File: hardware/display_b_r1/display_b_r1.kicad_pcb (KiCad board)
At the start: 2 copper layers, 155 x 54.5 mm, 1 part

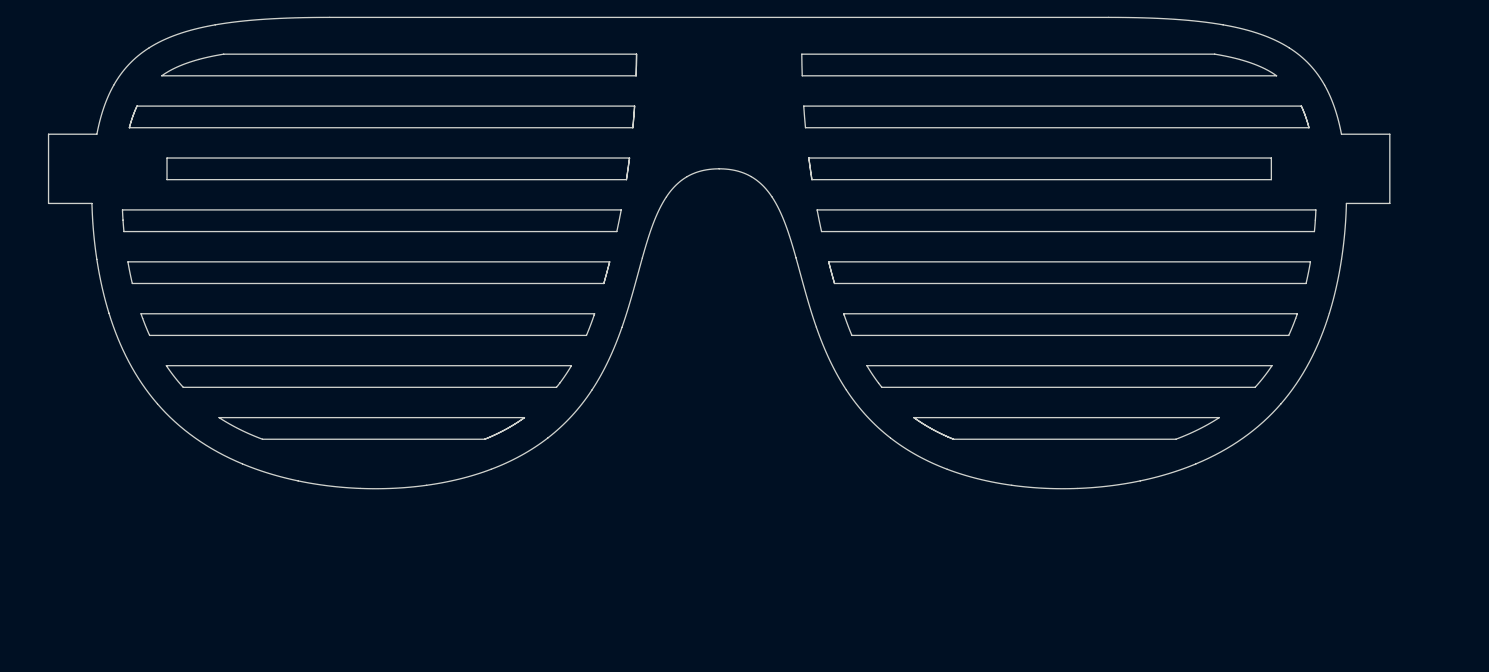
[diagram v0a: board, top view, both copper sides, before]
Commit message: Display board layout is now 95% complete, the number of caps on the board might need some further tweaking and there are also some gaps where a few more LEDs could fit. Additionally I've decided to provide the option to use the hinges as the ground connection allowing more +5V channels on the FFC connectors which should mean more current carrying capacity. The new power board schematic has had some changes, namely the vreg has changed and so have some of the passives around it, more input protect has been added, a MOV for over voltage protection and an NMOS for reverse pol. Looking at the new vreg the power dissipation before it cooks itself (~1.1W) isn't great but it's enough for about 2.5A (at around 93% eff.) for the LEDs which hasn't usually been the bottleneck (looking at you 9V batteries). This means we're expecting around 1.8A peak input current at a Vin of 7V and need to size the fuze around that as much more current and the vreg is cooked. Might look into a over voltage shutout circuit if it seems like we're blowing fuses too often.
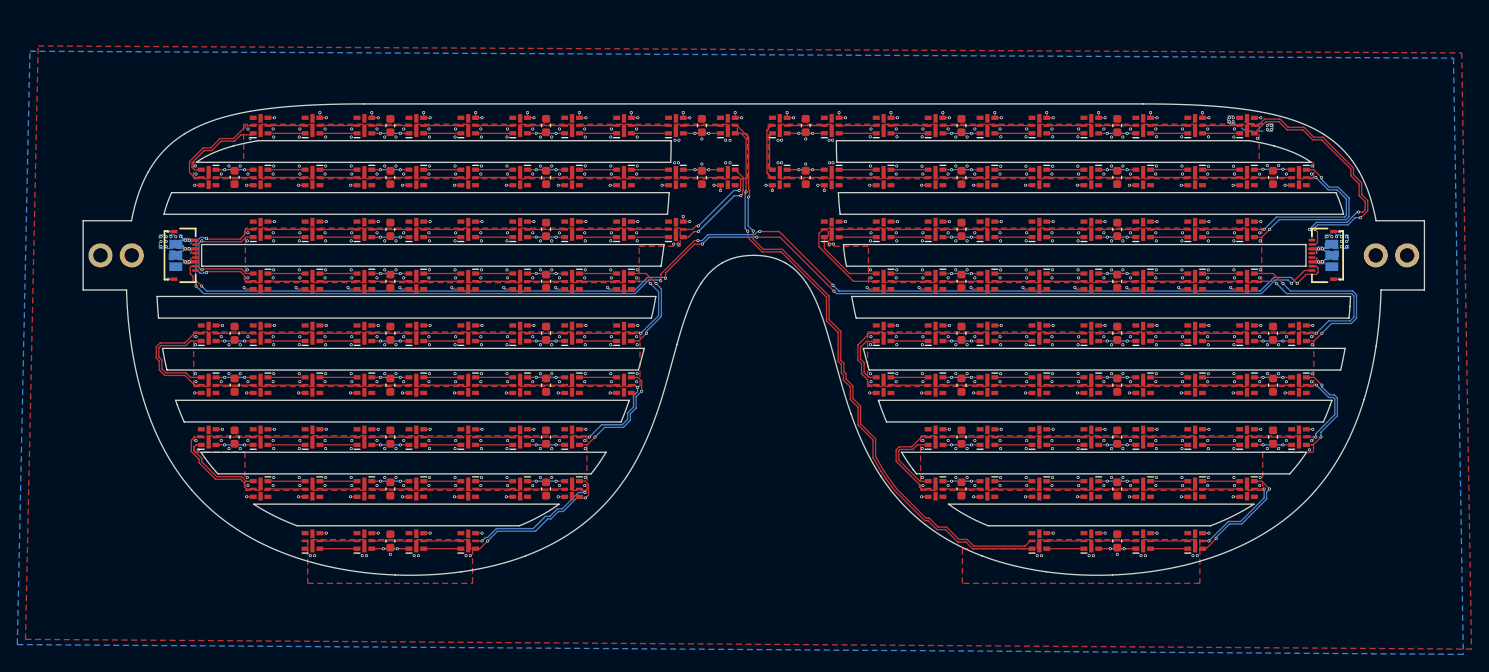
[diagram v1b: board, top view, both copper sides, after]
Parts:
- removed ?: , rave_shades:template_display_b_r1
- added C101: 22u 10V, Capacitor_SMD:C_0603_1608Metric, F.Cu at (108.0, 133.0)
- added C102: 22u 10V, Capacitor_SMD:C_0603_1608Metric, F.Cu at (192.0, 133.0)
- added C103: 22u 10V, Capacitor_SMD:C_0603_1608Metric, F.Cu at (210.0, 91.0)
- added C104: 22u 10V, Capacitor_SMD:C_0603_1608Metric, F.Cu at (108.0, 91.0)
- added C105: 22u 10V, Capacitor_SMD:C_0603_1608Metric, F.Cu at (108.0, 85.0)
- added C106: 22u 10V, Capacitor_SMD:C_0603_1608Metric, F.Cu at (108.0, 127.0)
- added C107: 22u 10V, Capacitor_SMD:C_0603_1608Metric, F.Cu at (108.0, 97.0)
- added C108: 22u 10V, Capacitor_SMD:C_0603_1608Metric, F.Cu at (108.0, 103.0)
- added C109: 22u 10V, Capacitor_SMD:C_0603_1608Metric, F.Cu at (108.0, 115.0)
- added C110: 22u 10V, Capacitor_SMD:C_0603_1608Metric, F.Cu at (192.0, 127.0)
- added C111: 22u 10V, Capacitor_SMD:C_0603_1608Metric, F.Cu at (108.0, 121.0)
- added C112: 22u 10V, Capacitor_SMD:C_0603_1608Metric, F.Cu at (192.0, 103.0)
- added C113: 22u 10V, Capacitor_SMD:C_0603_1608Metric, F.Cu at (192.0, 115.0)
- added C114: 22u 10V, Capacitor_SMD:C_0603_1608Metric, F.Cu at (108.0, 109.0)
- added C115: 22u 10V, Capacitor_SMD:C_0603_1608Metric, F.Cu at (192.0, 85.0)
- added C116: 22u 10V, Capacitor_SMD:C_0603_1608Metric, F.Cu at (192.0, 109.0)
- added C117: 22u 10V, Capacitor_SMD:C_0603_1608Metric, F.Cu at (192.0, 97.0)
- added C118: 22u 10V, Capacitor_SMD:C_0603_1608Metric, F.Cu at (192.0, 91.0)
- added C119: 22u 10V, Capacitor_SMD:C_0603_1608Metric, F.Cu at (192.0, 121.0)
- added C120: 22u 10V, Capacitor_SMD:C_0603_1608Metric, F.Cu at (174.0, 97.0)
- added C121: 22u 10V, Capacitor_SMD:C_0603_1608Metric, F.Cu at (210.0, 115.0)
- added C122: 22u 10V, Capacitor_SMD:C_0603_1608Metric, F.Cu at (174.0, 121.0)
- added C123: 22u 10V, Capacitor_SMD:C_0603_1608Metric, F.Cu at (126.0, 103.0)
- added C124: 22u 10V, Capacitor_SMD:C_0603_1608Metric, F.Cu at (126.0, 109.0)
- added C125: 22u 10V, Capacitor_SMD:C_0603_1608Metric, F.Cu at (144.0, 91.0)
- added C126: 22u 10V, Capacitor_SMD:C_0603_1608Metric, F.Cu at (90.0, 91.0)
- added C127: 22u 10V, Capacitor_SMD:C_0603_1608Metric, F.Cu at (126.0, 121.0)
- added C129: 22u 10V, Capacitor_SMD:C_0603_1608Metric, F.Cu at (90.0, 115.0)
- added C130: 22u 10V, Capacitor_SMD:C_0603_1608Metric, F.Cu at (174.0, 85.0)
- added C131: 22u 10V, Capacitor_SMD:C_0603_1608Metric, F.Cu at (174.0, 115.0)
- added C132: 22u 10V, Capacitor_SMD:C_0603_1608Metric, F.Cu at (174.0, 103.0)
- added C133: 22u 10V, Capacitor_SMD:C_0603_1608Metric, F.Cu at (126.0, 127.0)
- added C134: 22u 10V, Capacitor_SMD:C_0603_1608Metric, F.Cu at (126.0, 85.0)
- added C135: 22u 10V, Capacitor_SMD:C_0603_1608Metric, F.Cu at (156.0, 91.0)
- added C136: 22u 10V, Capacitor_SMD:C_0603_1608Metric, F.Cu at (126.0, 91.0)
- added C137: 22u 10V, Capacitor_SMD:C_0603_1608Metric, F.Cu at (156.0, 85.0)
- added C138: 22u 10V, Capacitor_SMD:C_0603_1608Metric, F.Cu at (90.0, 109.0)
- added C139: 22u 10V, Capacitor_SMD:C_0603_1608Metric, F.Cu at (174.0, 127.0)
- added C140: 22u 10V, Capacitor_SMD:C_0603_1608Metric, F.Cu at (90.0, 121.0)
- added C141: 22u 10V, Capacitor_SMD:C_0603_1608Metric, F.Cu at (210.0, 109.0)
- added C142: 22u 10V, Capacitor_SMD:C_0603_1608Metric, F.Cu at (126.0, 115.0)
- added C143: 22u 10V, Capacitor_SMD:C_0603_1608Metric, F.Cu at (174.0, 109.0)
- added C144: 22u 10V, Capacitor_SMD:C_0603_1608Metric, F.Cu at (126.0, 97.0)
- added C145: 22u 10V, Capacitor_SMD:C_0603_1608Metric, F.Cu at (210.0, 121.0)
- added C146: 22u 10V, Capacitor_SMD:C_0603_1608Metric, F.Cu at (144.0, 85.0)
- added C147: 22u 10V, Capacitor_SMD:C_0603_1608Metric, F.Cu at (174.0, 91.0)
- added D101: APA102-2020, rave_shades:LED-APA102-2020, F.Cu at (93.0, 85.0)
- added D102: APA102-2020, rave_shades:LED-APA102-2020, F.Cu at (87.0, 91.0)
- added D103: APA102-2020, rave_shades:LED-APA102-2020, F.Cu at (99.0, 97.0)
- added D104: APA102-2020, rave_shades:LED-APA102-2020, F.Cu at (93.0, 97.0)
- added D107: APA102-2020, rave_shades:LED-APA102-2020, F.Cu at (93.0, 127.0)
- added D108: APA102-2020, rave_shades:LED-APA102-2020, F.Cu at (99.0, 127.0)
- added D109: APA102-2020, rave_shades:LED-APA102-2020, F.Cu at (99.0, 85.0)
- added D110: APA102-2020, rave_shades:LED-APA102-2020, F.Cu at (93.0, 91.0)
- added D111: APA102-2020, rave_shades:LED-APA102-2020, F.Cu at (105.0, 97.0)
- added D112: APA102-2020, rave_shades:LED-APA102-2020, F.Cu at (93.0, 103.0)
- added D113: APA102-2020, rave_shades:LED-APA102-2020, F.Cu at (87.0, 109.0)
- added D114: APA102-2020, rave_shades:LED-APA102-2020, F.Cu at (87.0, 115.0)
- added D115: APA102-2020, rave_shades:LED-APA102-2020, F.Cu at (87.0, 121.0)
- added D116: APA102-2020, rave_shades:LED-APA102-2020, F.Cu at (105.0, 127.0)
- added D117: APA102-2020, rave_shades:LED-APA102-2020, F.Cu at (105.0, 85.0)
- added D118: APA102-2020, rave_shades:LED-APA102-2020, F.Cu at (99.0, 91.0)
- added D119: APA102-2020, rave_shades:LED-APA102-2020, F.Cu at (111.0, 97.0)
- added D120: APA102-2020, rave_shades:LED-APA102-2020, F.Cu at (99.0, 103.0)
- added D121: APA102-2020, rave_shades:LED-APA102-2020, F.Cu at (93.0, 109.0)
- added D122: APA102-2020, rave_shades:LED-APA102-2020, F.Cu at (93.0, 115.0)
- added D123: APA102-2020, rave_shades:LED-APA102-2020, F.Cu at (93.0, 121.0)
- added D124: APA102-2020, rave_shades:LED-APA102-2020, F.Cu at (111.0, 127.0)
- added D125: APA102-2020, rave_shades:LED-APA102-2020, F.Cu at (111.0, 85.0)
- added D126: APA102-2020, rave_shades:LED-APA102-2020, F.Cu at (105.0, 91.0)
- added D127: APA102-2020, rave_shades:LED-APA102-2020, F.Cu at (117.0, 97.0)
- added D128: APA102-2020, rave_shades:LED-APA102-2020, F.Cu at (105.0, 103.0)
- added D129: APA102-2020, rave_shades:LED-APA102-2020, F.Cu at (99.0, 109.0)
- added D130: APA102-2020, rave_shades:LED-APA102-2020, F.Cu at (99.0, 115.0)
- added D131: APA102-2020, rave_shades:LED-APA102-2020, F.Cu at (99.0, 121.0)
- added D132: APA102-2020, rave_shades:LED-APA102-2020, F.Cu at (117.0, 127.0)
- added D133: APA102-2020, rave_shades:LED-APA102-2020, F.Cu at (117.0, 85.0)
- added D134: APA102-2020, rave_shades:LED-APA102-2020, F.Cu at (111.0, 91.0)
- added D135: APA102-2020, rave_shades:LED-APA102-2020, F.Cu at (123.0, 97.0)
- added D136: APA102-2020, rave_shades:LED-APA102-2020, F.Cu at (111.0, 103.0)
- added D137: APA102-2020, rave_shades:LED-APA102-2020, F.Cu at (105.0, 109.0)
- added D138: APA102-2020, rave_shades:LED-APA102-2020, F.Cu at (105.0, 115.0)
- added D139: APA102-2020, rave_shades:LED-APA102-2020, F.Cu at (105.0, 121.0)
- added D140: APA102-2020, rave_shades:LED-APA102-2020, F.Cu at (123.0, 127.0)
- added D142: APA102-2020, rave_shades:LED-APA102-2020, F.Cu at (123.0, 85.0)
- added D143: APA102-2020, rave_shades:LED-APA102-2020, F.Cu at (117.0, 91.0)
- added D144: APA102-2020, rave_shades:LED-APA102-2020, F.Cu at (129.0, 97.0)
- added D145: APA102-2020, rave_shades:LED-APA102-2020, F.Cu at (117.0, 103.0)
- added D146: APA102-2020, rave_shades:LED-APA102-2020, F.Cu at (111.0, 109.0)
- added D147: APA102-2020, rave_shades:LED-APA102-2020, F.Cu at (111.0, 115.0)
- added D148: APA102-2020, rave_shades:LED-APA102-2020, F.Cu at (111.0, 121.0)
- added D149: APA102-2020, rave_shades:LED-APA102-2020, F.Cu at (129.0, 127.0)
- added D151: APA102-2020, rave_shades:LED-APA102-2020, F.Cu at (129.0, 85.0)
- added D152: APA102-2020, rave_shades:LED-APA102-2020, F.Cu at (123.0, 91.0)
- added D153: APA102-2020, rave_shades:LED-APA102-2020, F.Cu at (135.0, 97.0)
- added D154: APA102-2020, rave_shades:LED-APA102-2020, F.Cu at (123.0, 103.0)
- added D155: APA102-2020, rave_shades:LED-APA102-2020, F.Cu at (117.0, 109.0)
- added D156: APA102-2020, rave_shades:LED-APA102-2020, F.Cu at (117.0, 115.0)
- added D157: APA102-2020, rave_shades:LED-APA102-2020, F.Cu at (117.0, 121.0)
- added D158: APA102-2020, rave_shades:LED-APA102-2020, F.Cu at (117.0, 133.0)
- added D160: APA102-2020, rave_shades:LED-APA102-2020, F.Cu at (135.0, 85.0)
- added D161: APA102-2020, rave_shades:LED-APA102-2020, F.Cu at (129.0, 91.0)
- added D162: APA102-2020, rave_shades:LED-APA102-2020, F.Cu at (141.0, 97.0)
- added D163: APA102-2020, rave_shades:LED-APA102-2020, F.Cu at (129.0, 103.0)
- added D164: APA102-2020, rave_shades:LED-APA102-2020, F.Cu at (123.0, 109.0)
- added D165: APA102-2020, rave_shades:LED-APA102-2020, F.Cu at (123.0, 115.0)
- added D166: APA102-2020, rave_shades:LED-APA102-2020, F.Cu at (123.0, 121.0)
- added D167: APA102-2020, rave_shades:LED-APA102-2020, F.Cu at (111.0, 133.0)
- added D169: APA102-2020, rave_shades:LED-APA102-2020, F.Cu at (141.0, 85.0)
- added D170: APA102-2020, rave_shades:LED-APA102-2020, F.Cu at (135.0, 91.0)
- added D172: APA102-2020, rave_shades:LED-APA102-2020, F.Cu at (135.0, 103.0)
- added D173: APA102-2020, rave_shades:LED-APA102-2020, F.Cu at (129.0, 109.0)
- added D174: APA102-2020, rave_shades:LED-APA102-2020, F.Cu at (129.0, 115.0)
- added D175: APA102-2020, rave_shades:LED-APA102-2020, F.Cu at (129.0, 121.0)
- added D176: APA102-2020, rave_shades:LED-APA102-2020, F.Cu at (105.0, 133.0)
- added D178: APA102-2020, rave_shades:LED-APA102-2020, F.Cu at (147.0, 85.0)
- added D179: APA102-2020, rave_shades:LED-APA102-2020, F.Cu at (141.0, 91.0)
- added D180: APA102-2020, rave_shades:LED-APA102-2020, F.Cu at (147.0, 91.0)
- added D182: APA102-2020, rave_shades:LED-APA102-2020, F.Cu at (135.0, 109.0)
- added D183: APA102-2020, rave_shades:LED-APA102-2020, F.Cu at (135.0, 115.0)
- added D185: APA102-2020, rave_shades:LED-APA102-2020, F.Cu at (99.0, 133.0)
- added D187: APA102-2020, rave_shades:LED-APA102-2020, F.Cu at (153.0, 85.0)
- added D188: APA102-2020, rave_shades:LED-APA102-2020, F.Cu at (153.0, 91.0)
- added D189: APA102-2020, rave_shades:LED-APA102-2020, F.Cu at (159.0, 97.0)
- added D191: APA102-2020, rave_shades:LED-APA102-2020, F.Cu at (165.0, 109.0)
- added D192: APA102-2020, rave_shades:LED-APA102-2020, F.Cu at (165.0, 115.0)
- added D193: APA102-2020, rave_shades:LED-APA102-2020, F.Cu at (171.0, 127.0)
- added D194: APA102-2020, rave_shades:LED-APA102-2020, F.Cu at (177.0, 127.0)
- added D195: APA102-2020, rave_shades:LED-APA102-2020, F.Cu at (159.0, 85.0)
- added D196: APA102-2020, rave_shades:LED-APA102-2020, F.Cu at (159.0, 91.0)
- added D197: APA102-2020, rave_shades:LED-APA102-2020, F.Cu at (165.0, 97.0)
- added D199: APA102-2020, rave_shades:LED-APA102-2020, F.Cu at (171.0, 109.0)
- added D200: APA102-2020, rave_shades:LED-APA102-2020, F.Cu at (171.0, 115.0)
- added D202: APA102-2020, rave_shades:LED-APA102-2020, F.Cu at (183.0, 127.0)
- added D203: APA102-2020, rave_shades:LED-APA102-2020, F.Cu at (165.0, 85.0)
- added D204: APA102-2020, rave_shades:LED-APA102-2020, F.Cu at (165.0, 91.0)
- added D205: APA102-2020, rave_shades:LED-APA102-2020, F.Cu at (171.0, 97.0)
- added D206: APA102-2020, rave_shades:LED-APA102-2020, F.Cu at (165.0, 103.0)
- added D207: APA102-2020, rave_shades:LED-APA102-2020, F.Cu at (177.0, 109.0)
- added D208: APA102-2020, rave_shades:LED-APA102-2020, F.Cu at (177.0, 115.0)
- added D209: APA102-2020, rave_shades:LED-APA102-2020, F.Cu at (171.0, 121.0)
- added D210: APA102-2020, rave_shades:LED-APA102-2020, F.Cu at (189.0, 127.0)
- added D211: APA102-2020, rave_shades:LED-APA102-2020, F.Cu at (171.0, 85.0)
- added D212: APA102-2020, rave_shades:LED-APA102-2020, F.Cu at (171.0, 91.0)
- added D213: APA102-2020, rave_shades:LED-APA102-2020, F.Cu at (177.0, 97.0)
- added D214: APA102-2020, rave_shades:LED-APA102-2020, F.Cu at (171.0, 103.0)
- added D215: APA102-2020, rave_shades:LED-APA102-2020, F.Cu at (183.0, 109.0)
- added D216: APA102-2020, rave_shades:LED-APA102-2020, F.Cu at (183.0, 115.0)
- added D217: APA102-2020, rave_shades:LED-APA102-2020, F.Cu at (177.0, 121.0)
- added D218: APA102-2020, rave_shades:LED-APA102-2020, F.Cu at (195.0, 127.0)
- added D219: APA102-2020, rave_shades:LED-APA102-2020, F.Cu at (177.0, 85.0)
- added D220: APA102-2020, rave_shades:LED-APA102-2020, F.Cu at (177.0, 91.0)
- added D221: APA102-2020, rave_shades:LED-APA102-2020, F.Cu at (183.0, 97.0)
- added D222: APA102-2020, rave_shades:LED-APA102-2020, F.Cu at (177.0, 103.0)
- added D223: APA102-2020, rave_shades:LED-APA102-2020, F.Cu at (189.0, 109.0)
- added D224: APA102-2020, rave_shades:LED-APA102-2020, F.Cu at (189.0, 115.0)
- added D225: APA102-2020, rave_shades:LED-APA102-2020, F.Cu at (183.0, 121.0)
- added D226: APA102-2020, rave_shades:LED-APA102-2020, F.Cu at (201.0, 127.0)
- added D228: APA102-2020, rave_shades:LED-APA102-2020, F.Cu at (183.0, 85.0)
- added D229: APA102-2020, rave_shades:LED-APA102-2020, F.Cu at (183.0, 91.0)
- added D230: APA102-2020, rave_shades:LED-APA102-2020, F.Cu at (189.0, 97.0)
- added D231: APA102-2020, rave_shades:LED-APA102-2020, F.Cu at (183.0, 103.0)
- added D232: APA102-2020, rave_shades:LED-APA102-2020, F.Cu at (195.0, 109.0)
- added D233: APA102-2020, rave_shades:LED-APA102-2020, F.Cu at (195.0, 115.0)
- added D234: APA102-2020, rave_shades:LED-APA102-2020, F.Cu at (189.0, 121.0)
- added D235: APA102-2020, rave_shades:LED-APA102-2020, F.Cu at (207.0, 127.0)
- added D237: APA102-2020, rave_shades:LED-APA102-2020, F.Cu at (189.0, 85.0)
- added D238: APA102-2020, rave_shades:LED-APA102-2020, F.Cu at (189.0, 91.0)
- added D239: APA102-2020, rave_shades:LED-APA102-2020, F.Cu at (195.0, 97.0)
- added D240: APA102-2020, rave_shades:LED-APA102-2020, F.Cu at (189.0, 103.0)
- added D241: APA102-2020, rave_shades:LED-APA102-2020, F.Cu at (201.0, 109.0)
- added D242: APA102-2020, rave_shades:LED-APA102-2020, F.Cu at (201.0, 115.0)
- added D243: APA102-2020, rave_shades:LED-APA102-2020, F.Cu at (195.0, 121.0)
- added D244: APA102-2020, rave_shades:LED-APA102-2020, F.Cu at (201.0, 133.0)
- added D246: APA102-2020, rave_shades:LED-APA102-2020, F.Cu at (195.0, 85.0)
- added D247: APA102-2020, rave_shades:LED-APA102-2020, F.Cu at (195.0, 91.0)
- added D248: APA102-2020, rave_shades:LED-APA102-2020, F.Cu at (201.0, 97.0)
- added D249: APA102-2020, rave_shades:LED-APA102-2020, F.Cu at (195.0, 103.0)
- added D250: APA102-2020, rave_shades:LED-APA102-2020, F.Cu at (207.0, 109.0)
- added D251: APA102-2020, rave_shades:LED-APA102-2020, F.Cu at (207.0, 115.0)
- added D252: APA102-2020, rave_shades:LED-APA102-2020, F.Cu at (201.0, 121.0)
- added D253: APA102-2020, rave_shades:LED-APA102-2020, F.Cu at (195.0, 133.0)
- added D255: APA102-2020, rave_shades:LED-APA102-2020, F.Cu at (201.0, 85.0)
- added D256: APA102-2020, rave_shades:LED-APA102-2020, F.Cu at (201.0, 91.0)
- added D257: APA102-2020, rave_shades:LED-APA102-2020, F.Cu at (207.0, 97.0)
- added D258: APA102-2020, rave_shades:LED-APA102-2020, F.Cu at (201.0, 103.0)
- added D259: APA102-2020, rave_shades:LED-APA102-2020, F.Cu at (213.0, 109.0)
- added D260: APA102-2020, rave_shades:LED-APA102-2020, F.Cu at (213.0, 115.0)
- added D261: APA102-2020, rave_shades:LED-APA102-2020, F.Cu at (207.0, 121.0)
- added D262: APA102-2020, rave_shades:LED-APA102-2020, F.Cu at (189.0, 133.0)
- added D264: APA102-2020, rave_shades:LED-APA102-2020, F.Cu at (207.0, 85.0)
- added D265: APA102-2020, rave_shades:LED-APA102-2020, F.Cu at (207.0, 91.0)
- added D266: APA102-2020, rave_shades:LED-APA102-2020, F.Cu at (213.0, 91.0)
- added D267: APA102-2020, rave_shades:LED-APA102-2020, F.Cu at (207.0, 103.0)
- added D270: APA102-2020, rave_shades:LED-APA102-2020, F.Cu at (213.0, 121.0)
- added D271: APA102-2020, rave_shades:LED-APA102-2020, F.Cu at (183.0, 133.0)
- added H101: MountingHole_Pad, rave_shades:M1.4 Mounting Hole, F.Cu at (74.5, 100.0)
- added H102: MountingHole_Pad, rave_shades:M1.4 Mounting Hole, F.Cu at (78.1, 100.0)
- added H103: MountingHole_Pad, rave_shades:M1.4 Mounting Hole, F.Cu at (221.9, 100.0)
- added H104: MountingHole_Pad, rave_shades:M1.4 Mounting Hole, F.Cu at (225.5, 100.0)
- added J101: Conn_01x08, rave_shades:CF35082D0RE-NH, F.Cu at (85.5, 100.0)
- added J102: Conn_01x08, rave_shades:CF35082D0RE-NH, F.Cu at (214.5, 100.0)
- added JP101: SolderJumper_3_Open, Jumper:SolderJumper-3_P1.3mm_Open_Pad1.0x1.5mm, B.Cu at (83.2, 100.0)
- added JP102: SolderJumper_3_Open, Jumper:SolderJumper-3_P1.3mm_Open_Pad1.0x1.5mm, B.Cu at (216.8, 100.0)
- added Ref**: Val**, rave_shades:template_display_b_r1, F.Cu at (150.0, 100.0)
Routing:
- net /SPARE_0_5V0: track 0.00 -> 142.3 mm, vias 0 -> 6
- net /SPARE_1_5V0: track 0.00 -> 137.8 mm, vias 0 -> 6
- net GND: track 0.00 -> 134.4 mm, vias 0 -> 745
- net Net-(D178-Pad5): track 0.00 -> 69.6 mm, vias 0 -> 2
- net Net-(D178-Pad4): track 0.00 -> 69.0 mm, vias 0 -> 2
- net /LED_CLK_5V0: track 0.00 -> 29.2 mm, vias 0 -> 2
- net /LED_MOSI_5V0: track 0.00 -> 28.1 mm, vias 0 -> 2
- net Net-(D259-Pad4): track 0.00 -> 22.4 mm, vias 0 -> 2
- net Net-(D259-Pad5): track 0.00 -> 20.9 mm, vias 0 -> 2
- net Net-(D257-Pad4): track 0.00 -> 20.5 mm, vias 0 -> 2
- net Net-(D257-Pad5): track 0.00 -> 18.9 mm, vias 0 -> 2
- net Net-(D104-Pad2): track 0.00 -> 18.4 mm, vias 0 -> 2
- net Net-(D149-Pad3): track 0.00 -> 18.0 mm, vias 0 -> 2
- net Net-(D104-Pad3): track 0.00 -> 16.1 mm, vias 0 -> 2
- net Net-(D149-Pad2): track 0.00 -> 15.8 mm, vias 0 -> 2
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- added copper zone on B.Cu, net +5V
- added copper zone on F.Cu, net +5V
- added copper zone on B.Cu, net /5V0_OR_GND_1
- added copper zone on B.Cu, net /5V0_OR_GND_2
- added copper zone on B.Cu, net GND
- added copper zone on F.Cu, net GND
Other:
- outline, holes or cut-outs redrawn
